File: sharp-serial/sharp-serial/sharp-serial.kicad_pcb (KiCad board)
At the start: 2 copper layers, 47.4 x 30.5 mm, 2 parts, among them J1 sharp_connector_15pin, U1 FT232RL_breakout

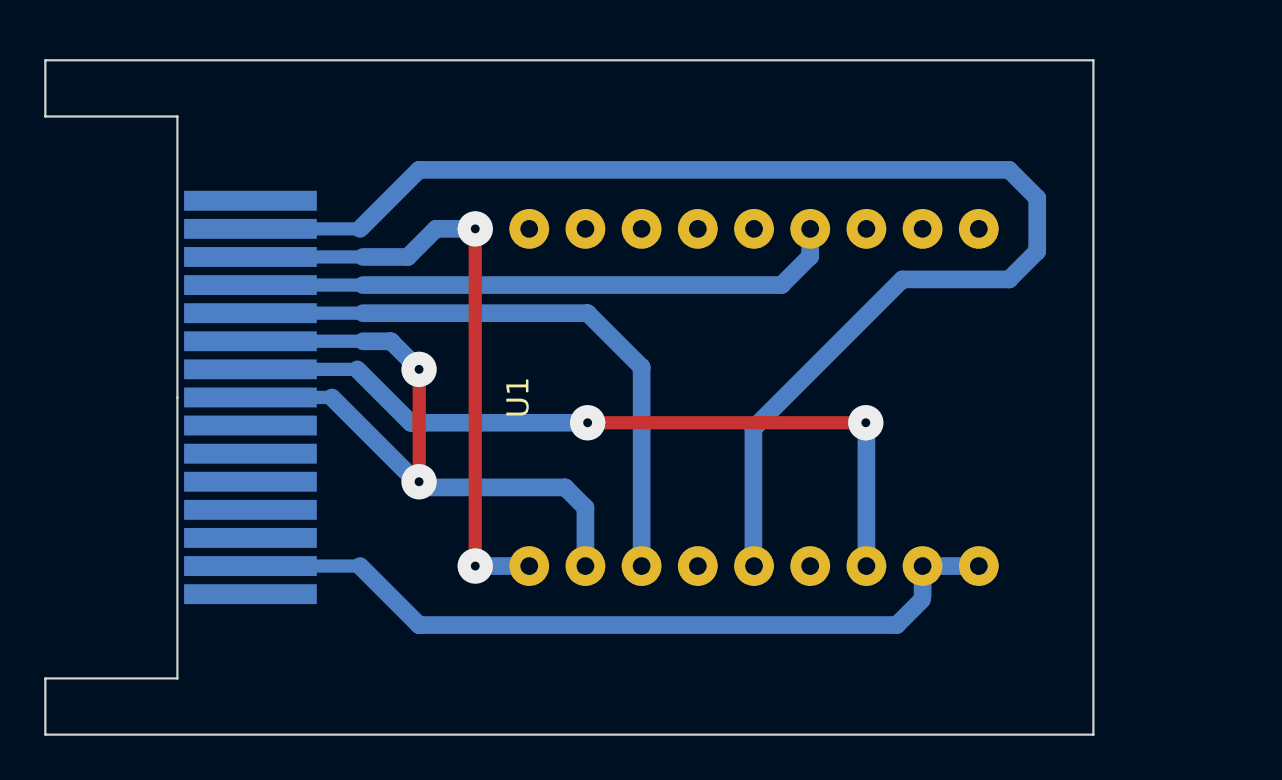
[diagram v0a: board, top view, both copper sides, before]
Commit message: USB->serial connector for Sharp using 6pins FT232RL cable
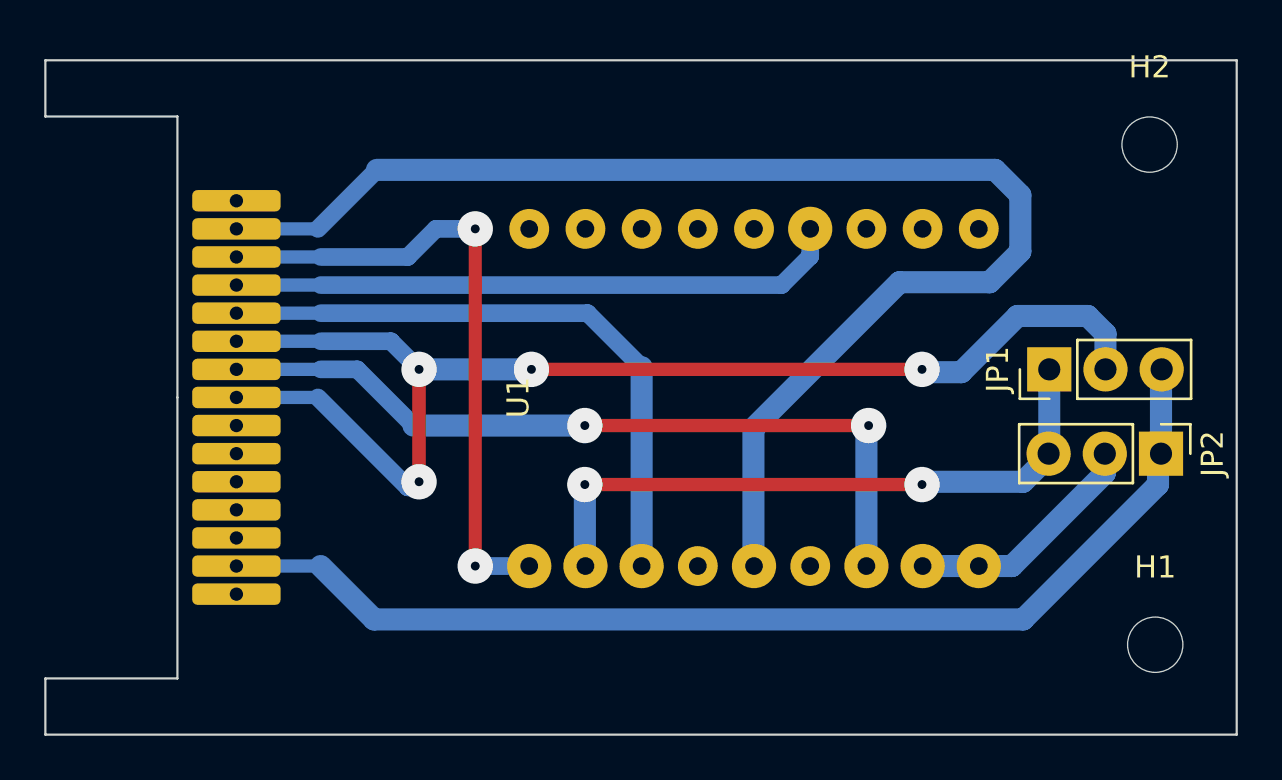
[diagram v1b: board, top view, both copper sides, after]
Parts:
- added H1: MountingHole, MountingHole:MountingHole_2.5mm, F.Cu at (167.9, 138.2)
- added H2: MountingHole, MountingHole:MountingHole_2.5mm, F.Cu at (167.6, 115.6)
- added JP1: Jumper_3_Bridged12, Connector_PinHeader_2.54mm:PinHeader_1x03_P2.54mm_Vertical, F.Cu at (163.1, 125.7)
- added JP2: Jumper_3_Bridged12, Connector_PinHeader_2.54mm:PinHeader_1x03_P2.54mm_Vertical, F.Cu at (168.2, 129.5)
- moved J1 0.64 mm to (126.4, 127.0)
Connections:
- J1 pad 6: Net-(U1-Pad2) -> Net-(J1-Pad6)
- J1 pad 8: Net-(U1-Pad2) -> Net-(J1-Pad6)
- U1 pad 2: Net-(U1-Pad2) -> Net-(JP1-Pad1)
- U1 pad 8: Net-(J1-Pad14) -> Net-(JP2-Pad2)
- U1 pad 9: Net-(J1-Pad14) -> Net-(JP2-Pad2)
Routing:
- net Net-(J1-Pad6): track 0.00 -> 56.4 mm, vias 0 -> 4
- net Net-(U1-Pad2): track 33.1 -> 0.00 mm, vias 2 -> 0
- net Net-(JP1-Pad1): track 0.00 -> 28.8 mm, vias 0 -> 2
- net Net-(J1-Pad14): track 36.0 -> 49.8 mm
- net Net-(JP2-Pad2): track 0.00 -> 10.9 mm
- net Net-(J1-Pad2): track 62.0 -> 60.5 mm
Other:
- board size 47.4 x 30.5 mm -> 53.8 x 30.5 mm
